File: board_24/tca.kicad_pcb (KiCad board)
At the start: 2 copper layers, 94.5 x 52 mm, 51 parts, among them IC1 ATMEGA328-A, P1 CONN_2, P2 CONN_3X2, P3 CONN_8X2, P4 CONN_8X2, P5 CONN_8X2, P6 CONN_8X2, P7 CONN_8X2, P8 CONN_8X2, Q1 BSS138, U1 TLC5941, U2 TLC5941, U3 TLC5941, U4 SD_CARD, U5 LD1117S50, U6 LD1117S33, Y1 RESONATEUR

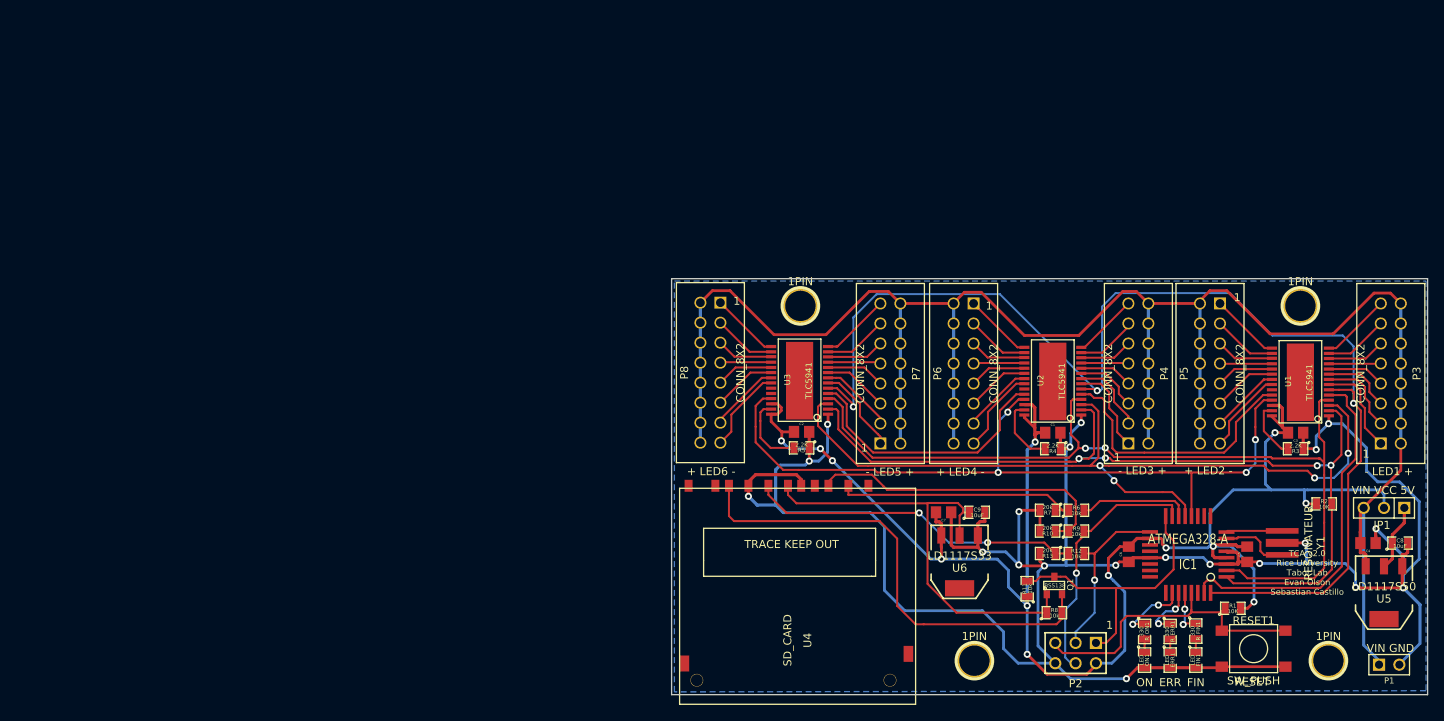
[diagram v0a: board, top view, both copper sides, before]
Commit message: Eliminated duplicate board_24 folder.
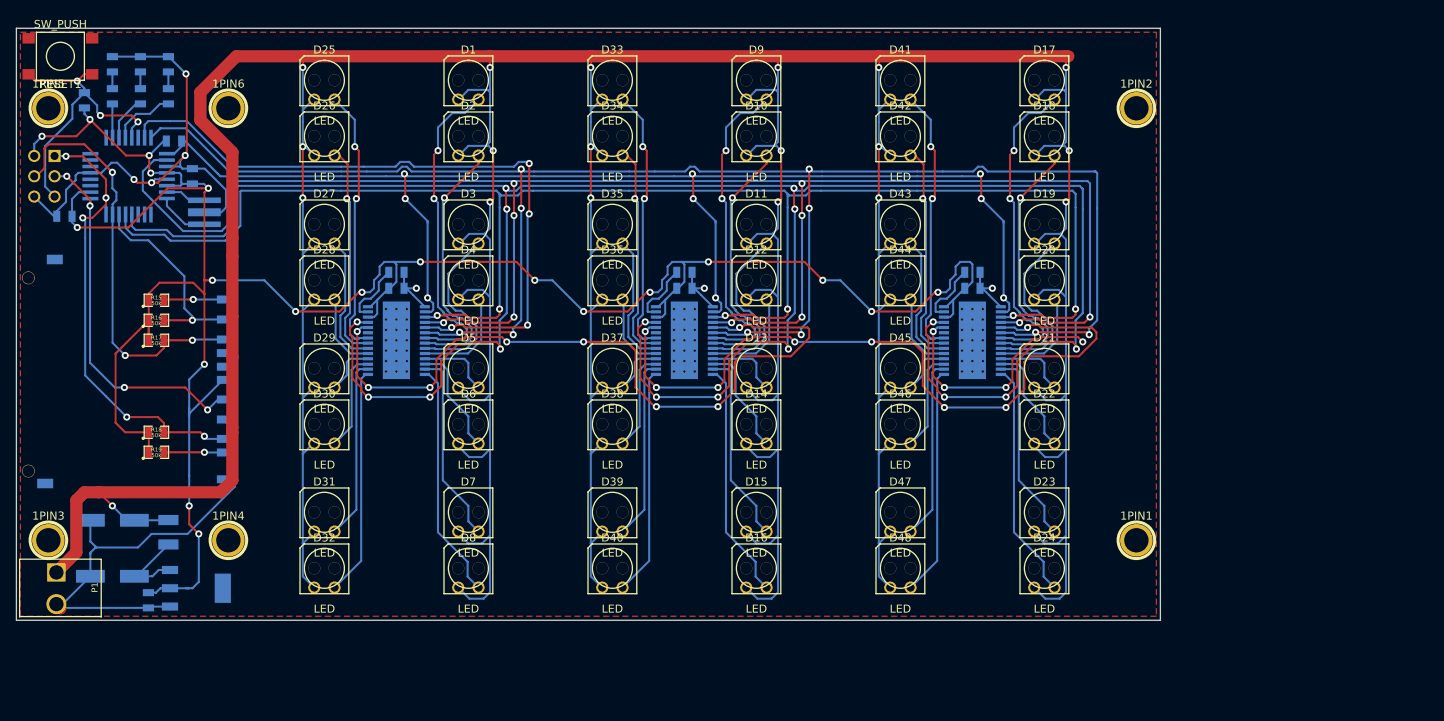
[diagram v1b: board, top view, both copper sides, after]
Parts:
- removed 1PIN (x4): P***, hole_ansi_6
- removed C9: 10uF, SM0805
- removed JP1: JUMPER3, PIN_ARRAY_3X1
- removed P3, P4, P5, P6, P7, P8: CONN_8X2, DF1B_8x2
- removed Q1: BSS138, SOT23
- removed R10, R13, R7: 20k, SM0805
- removed R11, R12, R6, R8, R9: 10k, SM0805
- removed U6: LD1117S33, SOT223
- added 1PIN1: P***, 1pin, F.Cu at (207.0, 158.5)
- added 1PIN2: P***, 1pin, F.Cu at (207.0, 104.5)
- added 1PIN3: P***, 1pin, F.Cu at (71.0, 158.5)
- added 1PIN4: P***, 1pin, F.Cu at (93.5, 158.5)
- added 1PIN5: P***, 1pin, F.Cu at (71.0, 104.5)
- added 1PIN6: P***, 1pin, F.Cu at (93.5, 104.5)
- added D1: LED, PCV220_LEDSOCKET, F.Cu at (123.5, 101.0)
- added D10: LED, PCV220_LEDSOCKET, F.Cu at (159.5, 108.0)
- added D11: LED, PCV220_LEDSOCKET, F.Cu at (159.5, 119.0)
- added D12: LED, PCV220_LEDSOCKET, F.Cu at (159.5, 126.0)
- added D13: LED, PCV220_LEDSOCKET, F.Cu at (159.5, 137.0)
- added D14: LED, PCV220_LEDSOCKET, F.Cu at (159.5, 144.0)
- added D15: LED, PCV220_LEDSOCKET, F.Cu at (159.5, 155.0)
- added D16: LED, PCV220_LEDSOCKET, F.Cu at (159.5, 162.0)
- added D17: LED, PCV220_LEDSOCKET, F.Cu at (195.5, 101.0)
- added D18: LED, PCV220_LEDSOCKET, F.Cu at (195.5, 108.0)
- added D19: LED, PCV220_LEDSOCKET, F.Cu at (195.5, 119.0)
- added D2: LED, PCV220_LEDSOCKET, F.Cu at (123.5, 108.0)
- added D20: LED, PCV220_LEDSOCKET, F.Cu at (195.5, 126.0)
- added D21: LED, PCV220_LEDSOCKET, F.Cu at (195.5, 137.0)
- added D22: LED, PCV220_LEDSOCKET, F.Cu at (195.5, 144.0)
- added D23: LED, PCV220_LEDSOCKET, F.Cu at (195.5, 155.0)
- added D24: LED, PCV220_LEDSOCKET, F.Cu at (195.5, 162.0)
- added D25: LED, PCV220_LEDSOCKET, F.Cu at (105.5, 101.0)
- added D26: LED, PCV220_LEDSOCKET, F.Cu at (105.5, 108.0)
- added D27: LED, PCV220_LEDSOCKET, F.Cu at (105.5, 119.0)
- added D28: LED, PCV220_LEDSOCKET, F.Cu at (105.5, 126.0)
- added D29: LED, PCV220_LEDSOCKET, F.Cu at (105.5, 137.0)
- added D3: LED, PCV220_LEDSOCKET, F.Cu at (123.5, 119.0)
- added D30: LED, PCV220_LEDSOCKET, F.Cu at (105.5, 144.0)
- added D31: LED, PCV220_LEDSOCKET, F.Cu at (105.5, 155.0)
- added D32: LED, PCV220_LEDSOCKET, F.Cu at (105.5, 162.0)
- added D33: LED, PCV220_LEDSOCKET, F.Cu at (141.5, 101.0)
- added D34: LED, PCV220_LEDSOCKET, F.Cu at (141.5, 108.0)
- added D35: LED, PCV220_LEDSOCKET, F.Cu at (141.5, 119.0)
- added D36: LED, PCV220_LEDSOCKET, F.Cu at (141.5, 126.0)
- added D37: LED, PCV220_LEDSOCKET, F.Cu at (141.5, 137.0)
- added D38: LED, PCV220_LEDSOCKET, F.Cu at (141.5, 144.0)
- added D39: LED, PCV220_LEDSOCKET, F.Cu at (141.5, 155.0)
- added D4: LED, PCV220_LEDSOCKET, F.Cu at (123.5, 126.0)
- added D40: LED, PCV220_LEDSOCKET, F.Cu at (141.5, 162.0)
- added D41: LED, PCV220_LEDSOCKET, F.Cu at (177.5, 101.0)
- added D42: LED, PCV220_LEDSOCKET, F.Cu at (177.5, 108.0)
- added D43: LED, PCV220_LEDSOCKET, F.Cu at (177.5, 119.0)
- added D44: LED, PCV220_LEDSOCKET, F.Cu at (177.5, 126.0)
- added D45: LED, PCV220_LEDSOCKET, F.Cu at (177.5, 137.0)
- added D46: LED, PCV220_LEDSOCKET, F.Cu at (177.5, 144.0)
- added D47: LED, PCV220_LEDSOCKET, F.Cu at (177.5, 155.0)
- added D48: LED, PCV220_LEDSOCKET, F.Cu at (177.5, 162.0)
- added D5: LED, PCV220_LEDSOCKET, F.Cu at (123.5, 137.0)
- added D6: LED, PCV220_LEDSOCKET, F.Cu at (123.5, 144.0)
- added D7: LED, PCV220_LEDSOCKET, F.Cu at (123.5, 155.0)
- added D8: LED, PCV220_LEDSOCKET, F.Cu at (123.5, 162.0)
- added D9: LED, PCV220_LEDSOCKET, F.Cu at (159.5, 101.0)
- added L1: 10uH, SM1210, B.Cu at (86.0, 157.5)
- added R15: 50k, SM0805, F.Cu at (84.5, 128.5)
- added R16: 50k, SM0805, F.Cu at (84.5, 131.0)
- added R17: 50k, SM0805, F.Cu at (84.5, 133.5)
- added R18: 50k, SM0805, F.Cu at (84.5, 145.0)
- added R19: 50k, SM0805, F.Cu at (84.5, 147.5)
- C1, C2, C6: footprint c_0805_FIXED -> SM0805; moved to B.Cu
- C3: value 0.1 uF -> 47uF; footprint c_0805_FIXED -> c_elec_6.3x5.3; moved to B.Cu
- C4: value 100nF -> 47uF; footprint c_0805_FIXED -> c_elec_6.3x5.3; moved to B.Cu
- C5: value 0.1 uF -> 10uF; footprint c_0805_FIXED -> SM0805; moved to B.Cu
- C7: value 100nF -> 0.1 uF; footprint c_0805_FIXED -> SM0805; moved to B.Cu
- C8: value 10uF -> 0.1 uF; moved to B.Cu
- ERR1, FIN1, IC1, ON1, P2, R1, R2, R3, R4, R5, R_ERR1, R_FIN1, R_ON1, Y1: moved to B.Cu
- P1: footprint PIN_ARRAY_2X1 -> PIN_ARRAY_2X1_3960um
- U1: value TLC5941 -> SD_CARD; footprint TLC5940_FIXED -> SD_CONN; moved to B.Cu
- U2: value TLC5941 -> LD1117S33; footprint TLC5940_FIXED -> SOT223; moved to B.Cu
- U3: footprint TLC5940_FIXED -> TLC5940_THERMVIAS2; moved to B.Cu
- U4: value SD_CARD -> TLC5941; footprint SD_CONN -> TLC5940_THERMVIAS2; moved to B.Cu
- U5: value LD1117S50 -> TLC5941; footprint SOT223 -> TLC5940_THERMVIAS2; moved to B.Cu
- moved P1 166.9 mm to (72.0, 164.5), turned to 270 degrees
- moved RESET1 166.5 mm to (72.5, 98.0), turned to 180 degrees
- moved U1 159.0 mm to (68.5, 137.0), turned to 180 degrees
- moved C4 157.0 mm to (79.0, 163.0), turned to 0 degrees
- moved R1 157.0 mm to (75.5, 103.5), turned to 270 degrees
- moved R2 150.8 mm to (86.7, 108.6), turned to 180 degrees
- moved ON1 149.0 mm to (79.0, 99.0), turned to 90 degrees
- moved ERR1 148.7 mm to (82.5, 99.0), turned to 90 degrees
- moved FIN1 148.5 mm to (86.0, 99.0), turned to 90 degrees
- moved C3 148.3 mm to (79.0, 156.0), turned to 0 degrees
- moved R_ON1 145.3 mm to (79.0, 103.0), turned to 90 degrees
- moved R_ERR1 145.1 mm to (82.5, 103.0), turned to 90 degrees
- moved R_FIN1 144.8 mm to (86.0, 103.0), turned to 90 degrees
- moved P2 142.0 mm to (70.5, 113.0), turned to 270 degrees
- moved Y1 140.9 mm to (90.5, 117.5), turned to 90 degrees
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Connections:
- C1 pad 2: /VCC -> /tlcs_1-3/VCC
- C2 pad 2: /VCC -> /tlcs_1-3/VCC
- C3 pad 1: /VCC -> /tlcs_1-3/VIN
- C4 pad 1: /VIN -> N-0000024
- C5 pad 1: /VCC -> /tlcs_1-3/VCC
- C6 pad 1: /VCC -> /tlcs_1-3/VCC
- C7 pad 1: /VCC -> /tlcs_1-3/VCC
- C8 pad 1: N-0000032 -> /tlcs_1-3/VCC
- IC1 pad 1: /BLANK -> /tlcs_1-3/BLANK
- IC1 pad 12: /GSCLK -> /tlcs_1-3/GSCLK
- IC1 pad 13: /XLAT -> /tlcs_1-3/XLAT
- IC1 pad 18: /VCC -> /tlcs_1-3/VCC
- IC1 pad 2: /SCLK -> /tlcs_1-3/SCLK
- IC1 pad 31: /SIN -> /tlcs_1-3/SIN
- IC1 pad 32: /MODE -> /tlcs_1-3/MODE
- IC1 pad 4: /VCC -> /tlcs_1-3/VCC
- IC1 pad 6: /VCC -> /tlcs_1-3/VCC
- P1 pad 1: /VIN -> /tlcs_1-3/VIN
- P2 pad 2: /VCC -> /tlcs_1-3/VCC
- R1 pad 2: /VCC -> /tlcs_1-3/VCC
- R2 pad 1: /VCC -> /tlcs_1-3/BLANK
- R2 pad 2: /BLANK -> /tlcs_1-3/VCC
- R3 pad 2: N-0000020 (its old number) -> N-0000086
- R4 pad 2: N-0000021 (its old number) -> N-0000087
- R5 pad 2: N-000003 -> N-0000088
- U1 pad 1: GND -> /SS
- U1 pad 2: /BLANK -> /MOSI
- U1 pad 3: /XLAT -> GND
- U1 pad 4: /SCLK -> /tlcs_1-3/VCC
- U1 pad 5: /SIN -> /SCK
- U1 pad 6: /MODE -> GND
- U1 pad 7: N-0000018 -> /MISO
- U2 pad 2: /BLANK -> /tlcs_1-3/VCC
- U2 pad 3: /XLAT -> N-0000024
- U2 pad 4: /SCLK -> (no net)
- U3 pad 2: /BLANK -> /tlcs_1-3/BLANK
- U3 pad 24: (no net) -> N-0000085
- U3 pad 25: /GSCLK -> /tlcs_1-3/GSCLK
- U3 pad 26: /VCC -> /tlcs_1-3/VCC
- U3 pad 27: N-000003 -> N-0000086
- U3 pad 28: /VCC -> /tlcs_1-3/VCC
- U3 pad 3: /XLAT -> /tlcs_1-3/XLAT
- U3 pad 4: /SCLK -> /tlcs_1-3/SCLK
- U3 pad 5: N-000002 -> /tlcs_1-3/SIN
- U3 pad 6: /MODE -> /tlcs_1-3/MODE
- U4 pad 1: /SD_CS -> GND
- U4 pad 2: /SD_DataIn -> /tlcs_1-3/BLANK
- U4 pad 3: GND -> /tlcs_1-3/XLAT
- U4 pad 4: /VSD -> /tlcs_1-3/SCLK
- U4 pad 5: /SD_SCLK -> N-0000085
- U4 pad 6: GND -> /tlcs_1-3/MODE
- U4 pad 7: /SD_DataOut -> N-0000055
- U4 pad 8: (no net) -> N-0000056
- U4 pad 9: (no net) -> N-0000057
- U5 pad 2: N-0000032 -> /tlcs_1-3/BLANK
- U5 pad 3: /VIN -> /tlcs_1-3/XLAT
- U5 pad 4: (no net) -> /tlcs_1-3/SCLK
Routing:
- net /tlcs_1-3/VIN: track 0.00 -> 763.1 mm, vias 0 -> 19
- net /tlcs_1-3/VCC: track 0.00 -> 309.7 mm, vias 0 -> 20
- net /tlcs_1-3/GSCLK: track 0.00 -> 290.9 mm, vias 0 -> 16
- net /VIN: track 249.6 -> 0.00 mm
- net /tlcs_1-3/MODE: track 0.00 -> 220.1 mm, vias 0 -> 10
- net /tlcs_1-3/SCLK: track 0.00 -> 218.0 mm, vias 0 -> 10
- net /VCC: track 203.5 -> 0.00 mm, vias 13 -> 0
- net /tlcs_1-3/XLAT: track 0.00 -> 202.6 mm, vias 0 -> 6
- net /tlcs_1-3/BLANK: track 0.00 -> 164.1 mm, vias 0 -> 9
- net GND: track 308.8 -> 152.8 mm, vias 20 -> 7
- net /MODE: track 152.0 -> 0.00 mm, vias 3 -> 0
- net /BLANK: track 112.9 -> 0.00 mm, vias 4 -> 0
- net /SCLK: track 111.1 -> 0.00 mm, vias 2 -> 0
- net /XLAT: track 106.3 -> 0.00 mm, vias 4 -> 0
- net /GSCLK: track 97.7 -> 0.00 mm, vias 4 -> 0
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- added copper zone on F.Cu, net GND
- removed copper zone on B.Cu, net GND
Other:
- board size 94.5 x 52 mm -> 143 x 74 mm
- board text removed: "+ LED2 -"
- board text removed: "+ LED4 -"
- board text removed: "+ LED6 -"
- board text removed: "- LED1 +"
- board text removed: "- LED3 +"
- board text removed: "- LED5 +"
- board text removed: "1"
- board text removed: "RESET"
- board text removed: "TCA v2.0 Rice University Tabor Lab Evan Olson Sebastian Castillo"
- board text removed: "VIN GND"
- board text removed: "VIN VCC 5V"
